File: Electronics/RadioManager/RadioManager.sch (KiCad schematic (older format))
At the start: 21 parts

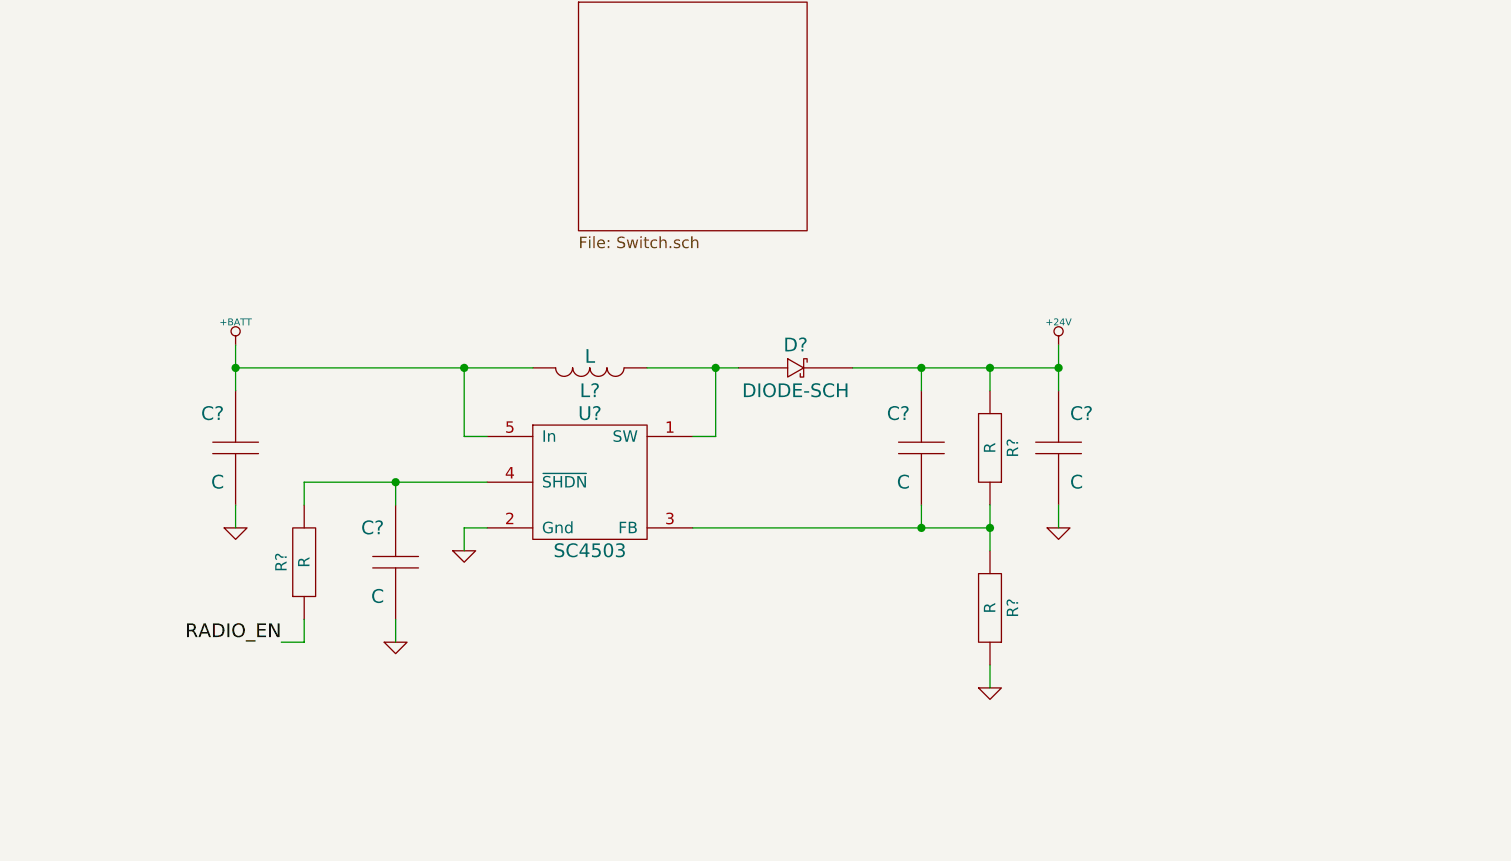
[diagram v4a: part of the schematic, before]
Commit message: Move power to new page
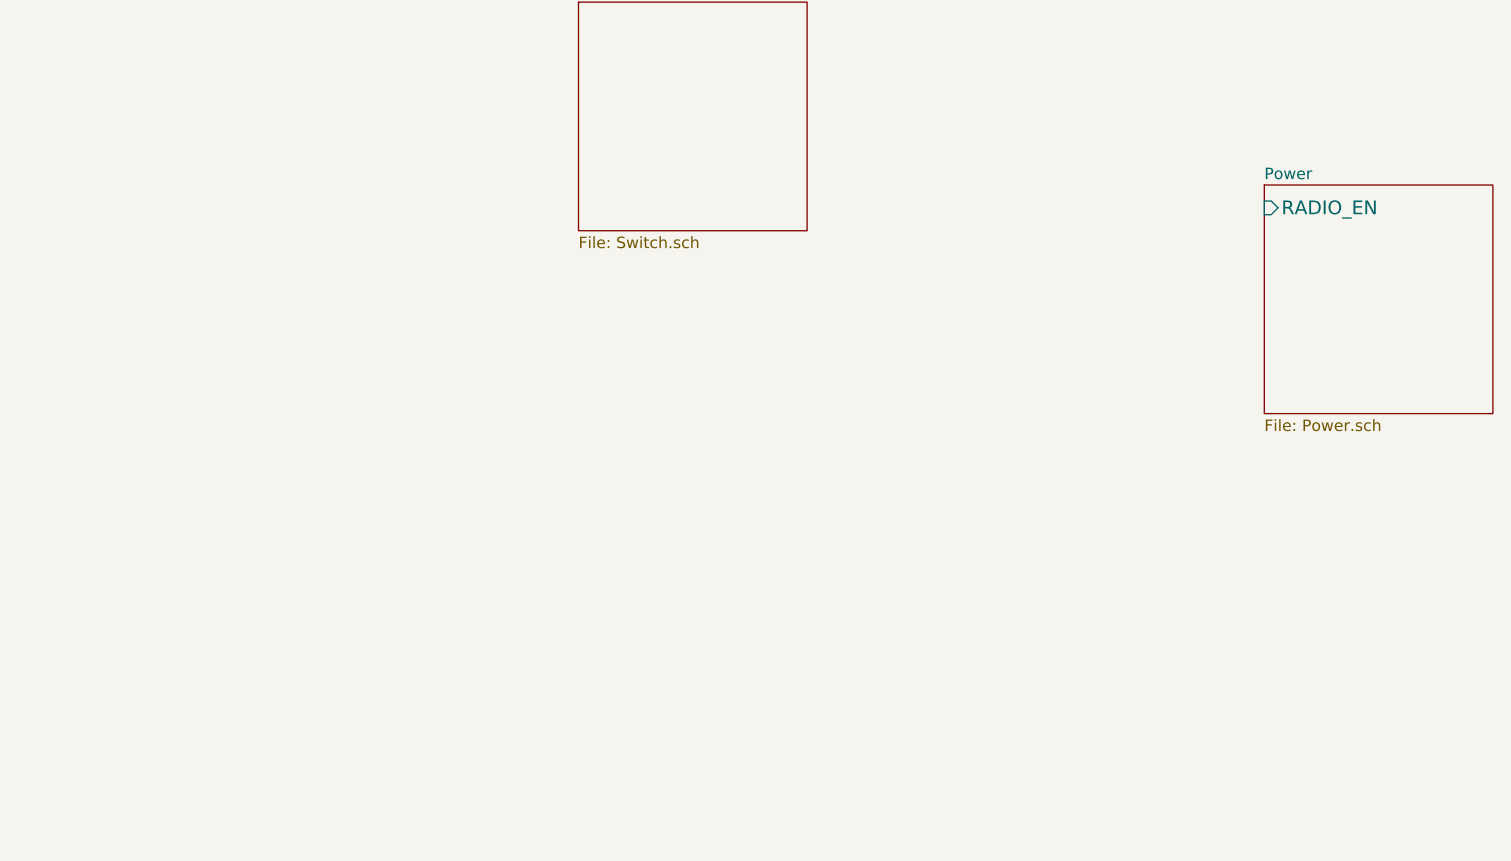
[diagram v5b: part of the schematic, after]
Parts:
- removed C? (x4): C, ~, symbol C
- removed D?: DIODE-SCH, ~, symbol DIODE-SCH
- removed L?: L, ~, symbol L
- removed R? (x3): R, ~, symbol R
- removed U?: SC4503, symbol SC4503

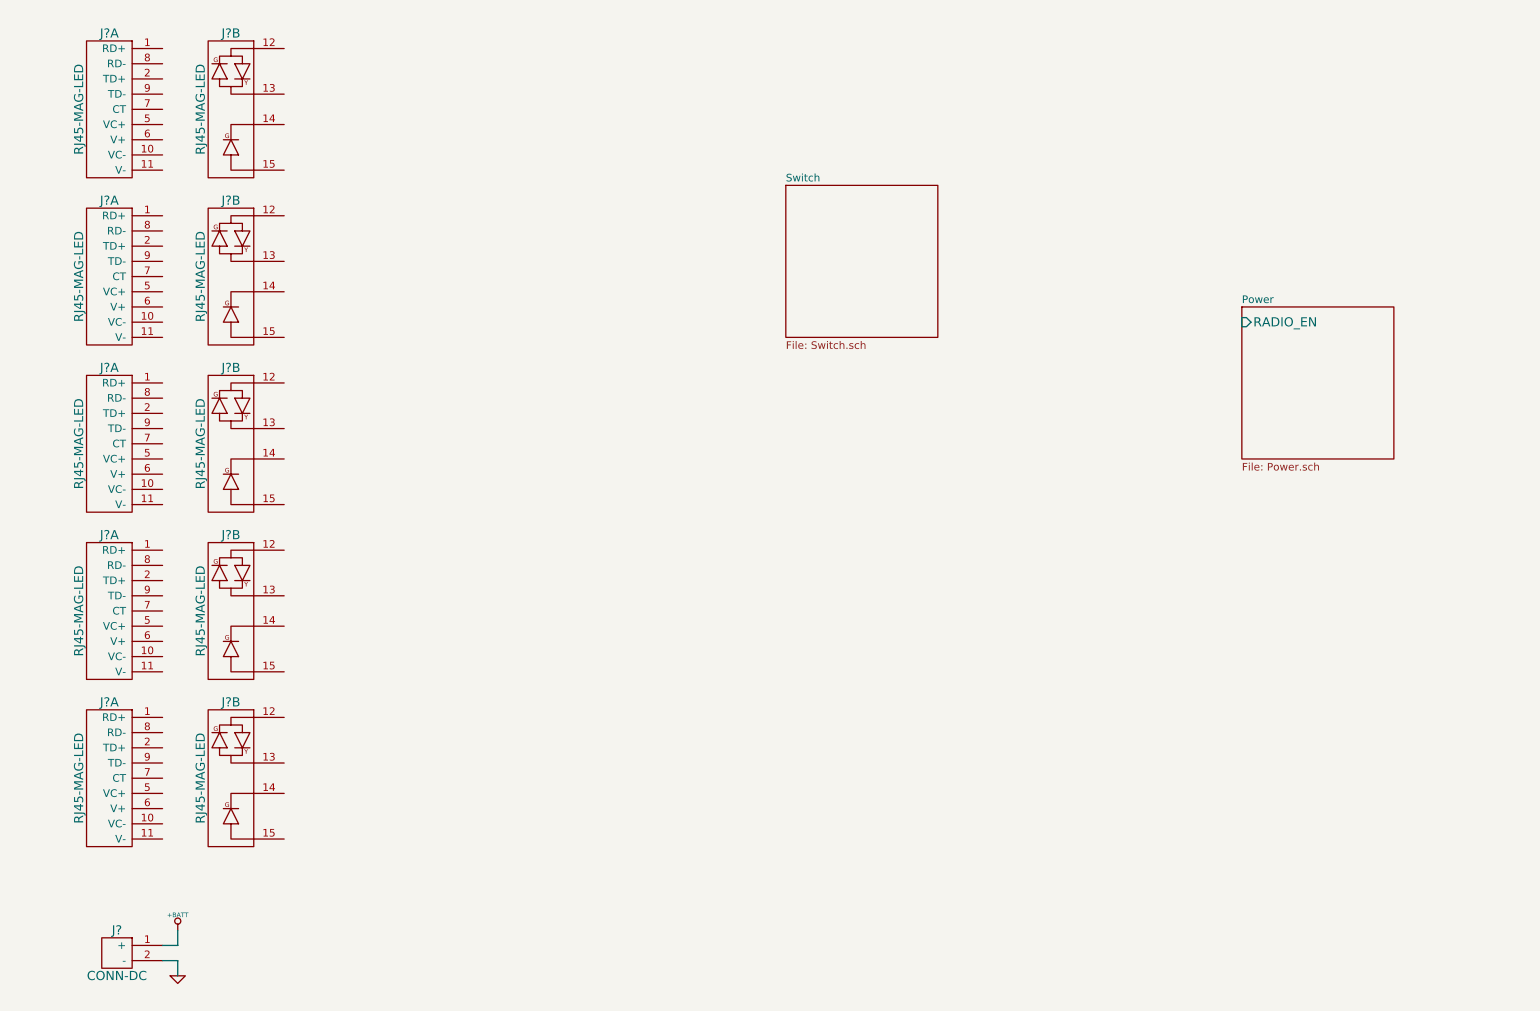
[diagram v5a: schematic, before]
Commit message: Wire RJ45 jacks
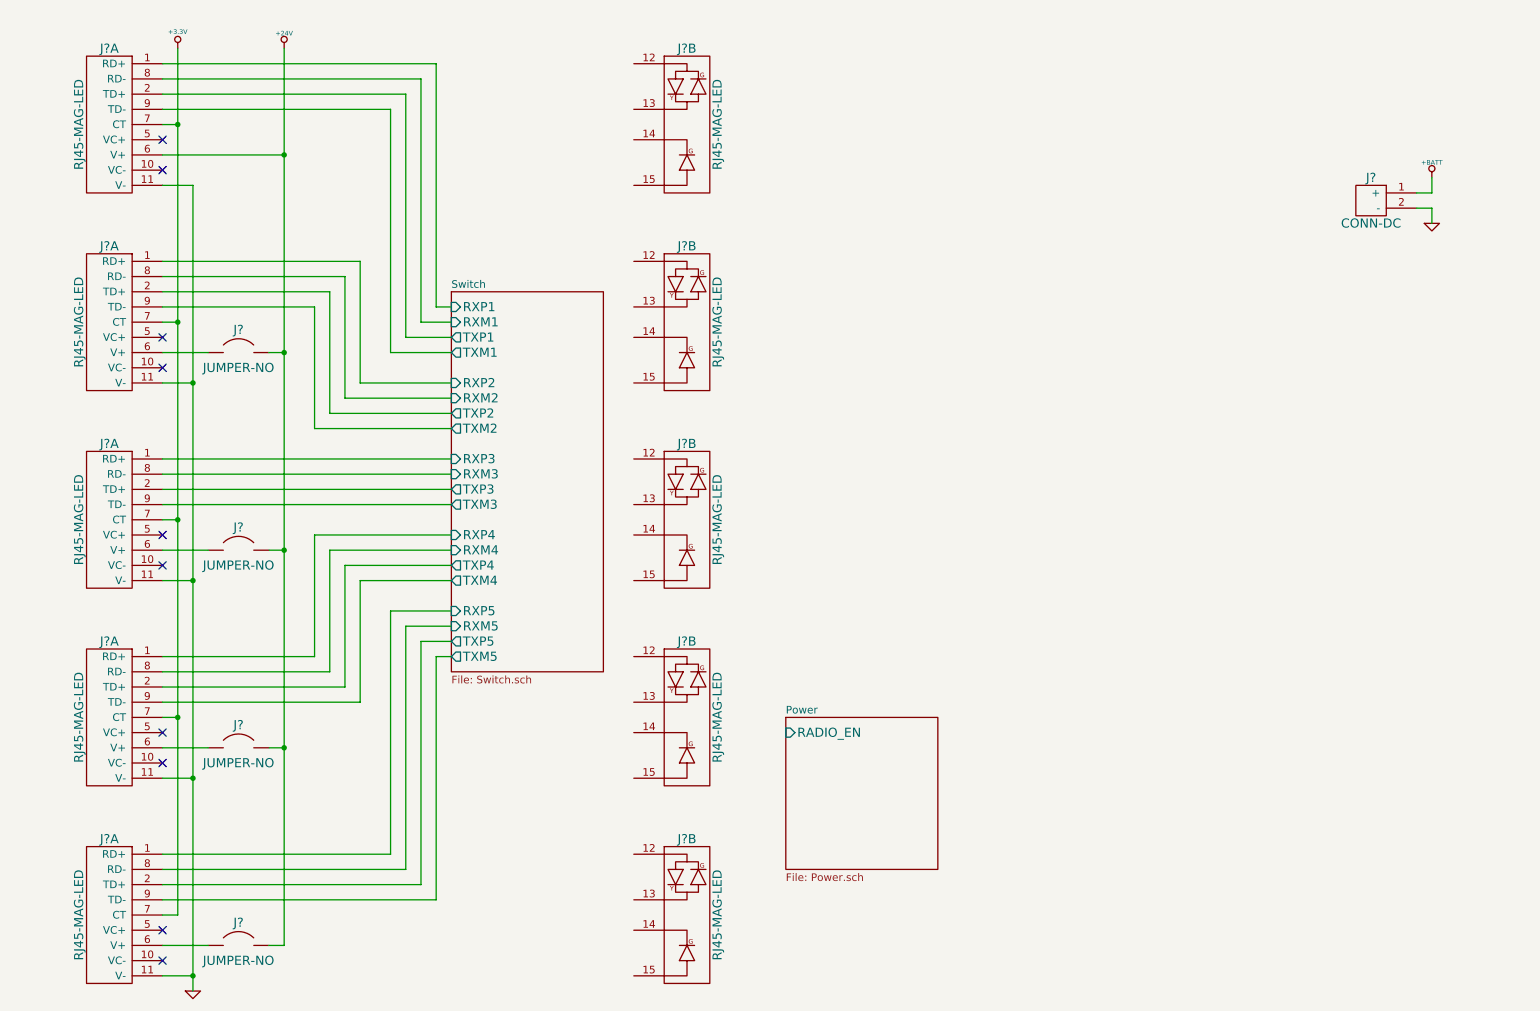
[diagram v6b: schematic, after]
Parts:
- added J? (x4): JUMPER-NO, ~, symbol JUMPER-NO
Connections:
- net GND: now also J?.11 (V-), J?.11 (V-), J?.11 (V-), J?.11 (V-), J?.11 (V-)
- net Switch/RXP1: now reaches J?.1 (RD+)
- net Switch/TXP1: now reaches J?.2 (TD+)
- net +24V: now reaches J?.6 (V+)
- net +24V: now also J?.2, J?.2, J?.2, J?.2
- net +3.3V: now reaches J?.7 (CT)
- net +3.3V: now also J?.7 (CT), J?.7 (CT), J?.7 (CT), J?.7 (CT)
- net Switch/RXM1: now reaches J?.8 (RD-)
- net Switch/TXM1: now reaches J?.9 (TD-)
- net Switch/RXP2: now reaches J?.1 (RD+)
- net Switch/TXP2: now reaches J?.2 (TD+)
- net at J?.6 (V+): now also J?.1 (x4)
- net Switch/RXM2: now reaches J?.8 (RD-)
- net Switch/TXM2: now reaches J?.9 (TD-)
- net Switch/RXP3: now reaches J?.1 (RD+)
- net Switch/TXP3: now reaches J?.2 (TD+)
- net Switch/RXM3: now reaches J?.8 (RD-)
- net Switch/TXM3: now reaches J?.9 (TD-)
- net Switch/RXP4: now reaches J?.1 (RD+)
- net Switch/TXP4: now reaches J?.2 (TD+)
- net Switch/RXM4: now reaches J?.8 (RD-)
- net Switch/TXM4: now reaches J?.9 (TD-)
- net Switch/RXP5: now reaches J?.1 (RD+)
- net Switch/TXP5: now reaches J?.2 (TD+)
- net Switch/RXM5: now reaches J?.8 (RD-)
- net Switch/TXM5: now reaches J?.9 (TD-)
- no-connect marks 0 -> 10
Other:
- moved on the sheet: J?, J?A, J?B
